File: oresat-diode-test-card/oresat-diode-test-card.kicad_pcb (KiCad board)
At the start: 4 copper layers, 99.8 x 94.6 mm, 140 parts, among them J6 J-SAMTEC-TFM-120-X1-XXX-D-RA, J7 ORESAT-DEBUG-CONNECTOR-ALL, Q1 DMP2240UDM, Q2 DMP3050LVT-7, Q4 DMP3050LVT-7, Q5 PMV45EN, Q7 MOSFET-PCH-SOT23-6, Q8 PMV45EN, Q9 PMV45EN, U1 TCAN330, U10 TPS62111RSA, U11 MIC842LYC5, U12 MIC842LYC5, U13 TLV6001DCK, U2 MAX7310, U3 TS5A21366DCUR, U4 TLV6001DCK, U6 MAX4211, U7 STM32F091C, U8 NX3L4051-Q100, U9 TLV6001DCK, X2 CRYSTAL-WITH-GND

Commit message: another layout rev
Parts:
- moved C6 14.5 mm to (135.3, 106.3), turned to 90 degrees
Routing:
- net Net-(D1-A): track 0.00 -> 78.3 mm, vias 0 -> 3
- net 3.3V: track 10.2 -> 73.0 mm, vias 13 -> 19
- net Net-(U5-1460nm): track 0.00 -> 39.2 mm, vias 0 -> 2
- net Net-(U5-1550nm): track 0.00 -> 38.6 mm, vias 0 -> 3
- net Net-(U5-1300nm): track 0.00 -> 31.8 mm
- net Net-(U5-1200nm): track 0.00 -> 30.5 mm, vias 0 -> 2
- net Net-(U5-1040nm): track 0.00 -> 28.9 mm, vias 0 -> 2
- net Net-(D2-K): track 9.52 -> 31.3 mm
- net Net-(D4-K): track 11.2 -> 26.5 mm
- net LED_CURRENT: track 61.8 -> 76.6 mm, vias 2 -> 3
- net Net-(U5-PD_Cathode): track 0.00 -> 9.51 mm
- net Net-(D1-K): track 12.2 -> 19.4 mm
- net SWIR_PD_CURRENT: track 68.9 -> 75.2 mm
- net ~{LED_MUX_ENABLE}: track 93.4 -> 90.4 mm
- net Net-(D8-K): track 2.63 -> 5.00 mm
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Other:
- board text added: "*:.｡.o(≧▽≦)o.｡.:*"
- board text added: "HAVE FUN! <3"
- board text added: "k"
- board text added: "m"
- board text added: "ori"
- board text added: "s"

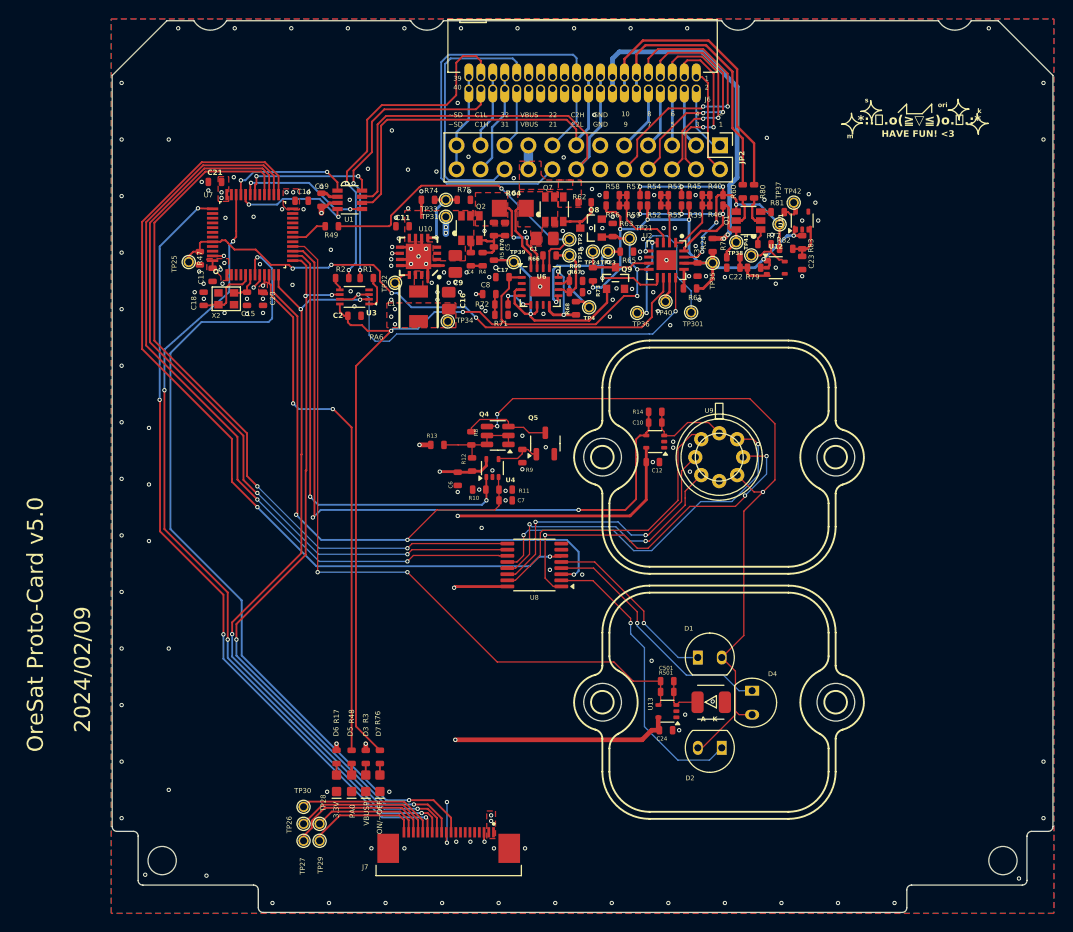
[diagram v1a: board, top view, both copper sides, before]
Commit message: Fix DRCs, clean up some routing, fix footprint movement on OPD.
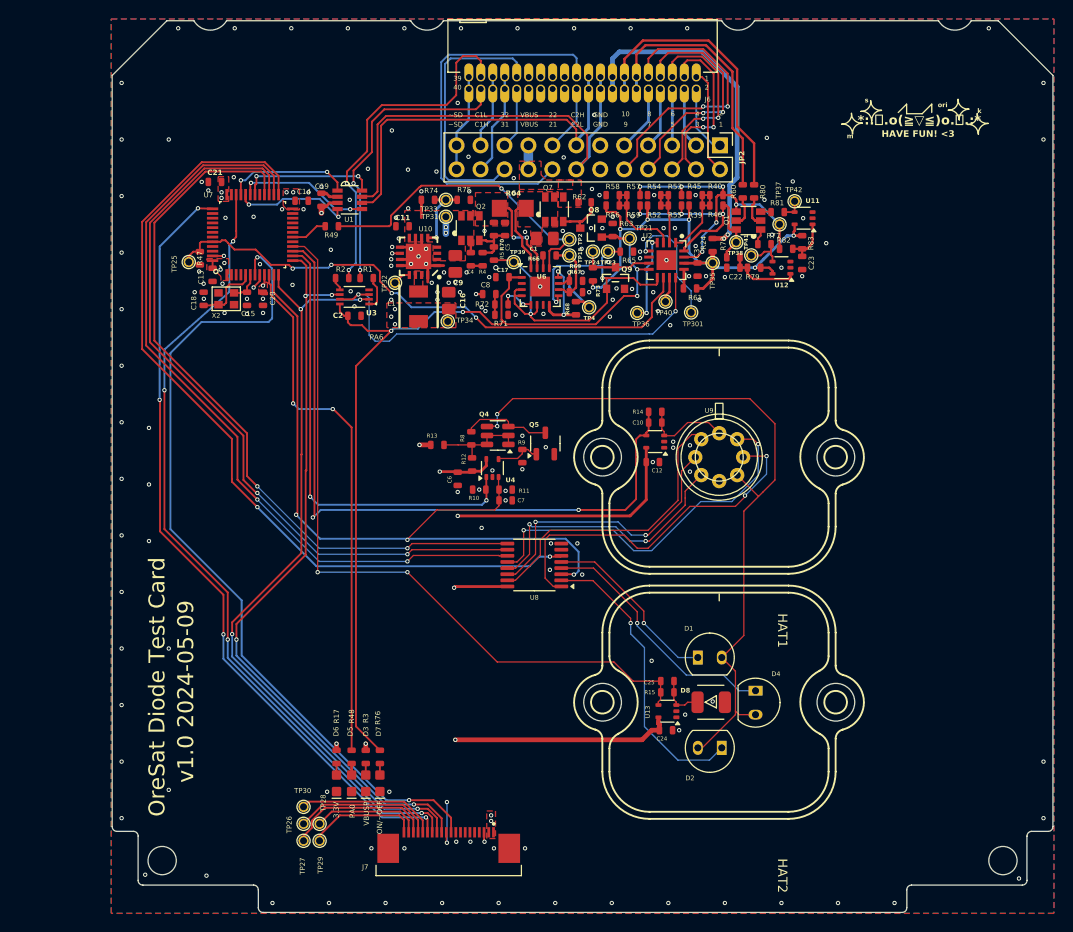
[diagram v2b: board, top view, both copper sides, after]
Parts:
- removed C501: 100n, oresat-passives:0603-C-NOSILK
- removed R501: 10K, oresat-passives:0603-C-NOSILK
- added C25: 100n, oresat-passives:0603-C-NOSILK, F.Cu at (157.5, 128.9)
- added R15: 10K, oresat-passives:0603-C-NOSILK, F.Cu at (157.5, 127.8)
- moved U12 0.60 mm to (169.6, 83.9), turned to 180 degrees
- moved D4 0.36 mm to (166.8, 128.8)
- moved U11 0.29 mm to (171.9, 78.7), turned to 180 degrees
- moved TP42 0.18 mm to (171.0, 76.8)
- renumbered REF** to HAT1, REF** to HAT2
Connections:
- Q9 pad 1: /Power/CB_CTRL -> /Power/CB-RESET
- R5 pad 1: /Power/CB_CTRL -> /Power/CB-RESET
- TP39 pad 1: /Power/CB_CTRL -> /Power/CB-RESET
- U6 pad 3: /Power/CB_CTRL -> /Power/CB-RESET
- U6 pad 4: /Power/CB_CTRL -> /Power/CB-RESET
- U6 pad 6: /Power/CB_CTRL -> /Power/CB-RESET
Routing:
- net /Power/CB-RESET: track 20.8 -> 48.1 mm, vias 2 -> 3
- net /Power/CB_CTRL: track 26.1 -> 0.00 mm, vias 1 -> 0
- net Net-(U12-INP): track 4.95 -> 7.73 mm
- net Net-(U5-1550nm): track 38.6 -> 38.4 mm, vias 3 -> 2
- net Net-(D1-A): track 78.3 -> 78.4 mm, vias 3 -> 2
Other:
- board text added: "${REVISION} ${ISSUE_DATE}"
- board text added: "OreSat Diode Test Card"
- board text removed: "2024/02/09"
- board text removed: "A K"
- board text removed: "OreSat Proto-Card v5.0"

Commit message: added test points and trace width edits
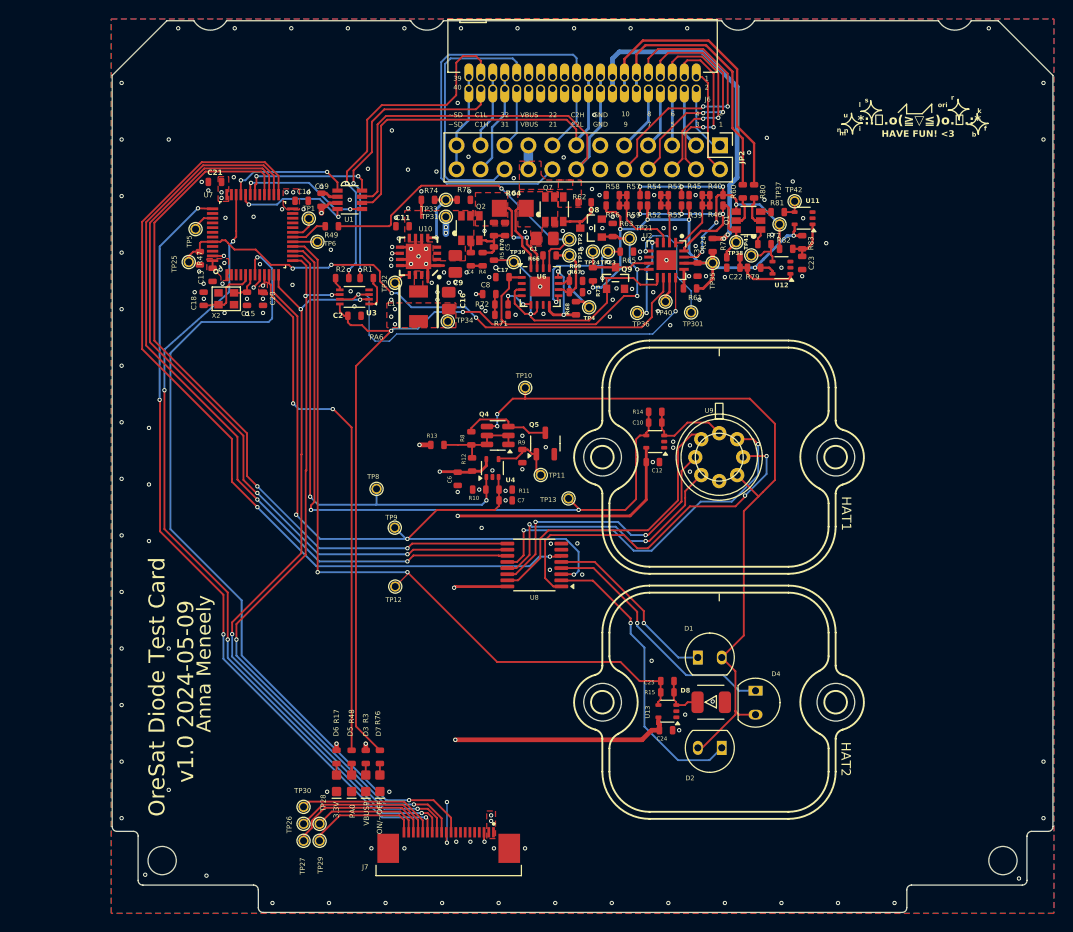
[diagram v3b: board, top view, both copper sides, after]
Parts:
- added TP1: TEST-POINT-LARGE-SQUARE, oresat-proto-card:1X01, F.Cu at (119.5, 78.7)
- added TP10: TEST-POINT-LARGE-SQUARE, oresat-proto-card:1X01, F.Cu at (142.4, 96.6)
- added TP11: TEST-POINT-LARGE-SQUARE, oresat-proto-card:1X01, F.Cu at (144.1, 105.9)
- added TP12: TEST-POINT-LARGE-SQUARE, oresat-proto-card:1X01, F.Cu at (128.6, 117.7)
- added TP13: TEST-POINT-LARGE-SQUARE, oresat-proto-card:1X01, F.Cu at (147.0, 108.4)
- added TP5: TEST-POINT-LARGE-SQUARE, oresat-proto-card:1X01, F.Cu at (107.4, 79.8)
- added TP6: TEST-POINT-LARGE-SQUARE, oresat-proto-card:1X01, F.Cu at (120.4, 81.2)
- added TP8: TEST-POINT-LARGE-SQUARE, oresat-proto-card:1X01, F.Cu at (126.6, 107.4)
- added TP9: TEST-POINT-LARGE-SQUARE, oresat-proto-card:1X01, F.Cu at (128.6, 111.5)
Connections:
- U7 pad 17: unconnected-(U7-PA7-Pad17) -> Net-(U7-PA7)
- U7 pad 19: unconnected-(U7-PB1-Pad19) -> Net-(U7-PB1)
- U7 pad 39: unconnected-(U7-PB3-Pad39) -> Net-(U7-PB3)
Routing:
- net Net-(U7-PB1): track 0.00 -> 2.80 mm
- net Net-(U7-PA7): track 0.00 -> 2.62 mm
- net Net-(U7-PB3): track 0.00 -> 2.45 mm
- net Net-(Q5-G): track 4.90 -> 7.23 mm
- net UV_PD_CURRENT: track 80.2 -> 82.2 mm
- net LED_CURRENT: track 76.6 -> 78.4 mm
- net DAC_OUT: track 48.7 -> 50.4 mm
- net Net-(D1-A): track 78.4 -> 79.5 mm
- net SWIR_PD_CURRENT: track 75.2 -> 76.0 mm
- net GND: vias 188 -> 189
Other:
- board text added: "Anna Meneely"
- board text added: "b"
- board text added: "f"
- board text added: "i"
- board text added: "l"
- board text added: "n"
- board text added: "r"
- board text added: "u"

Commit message: Fix OPD weirdness, lots of little polishing including power plane movement and thicker traces.
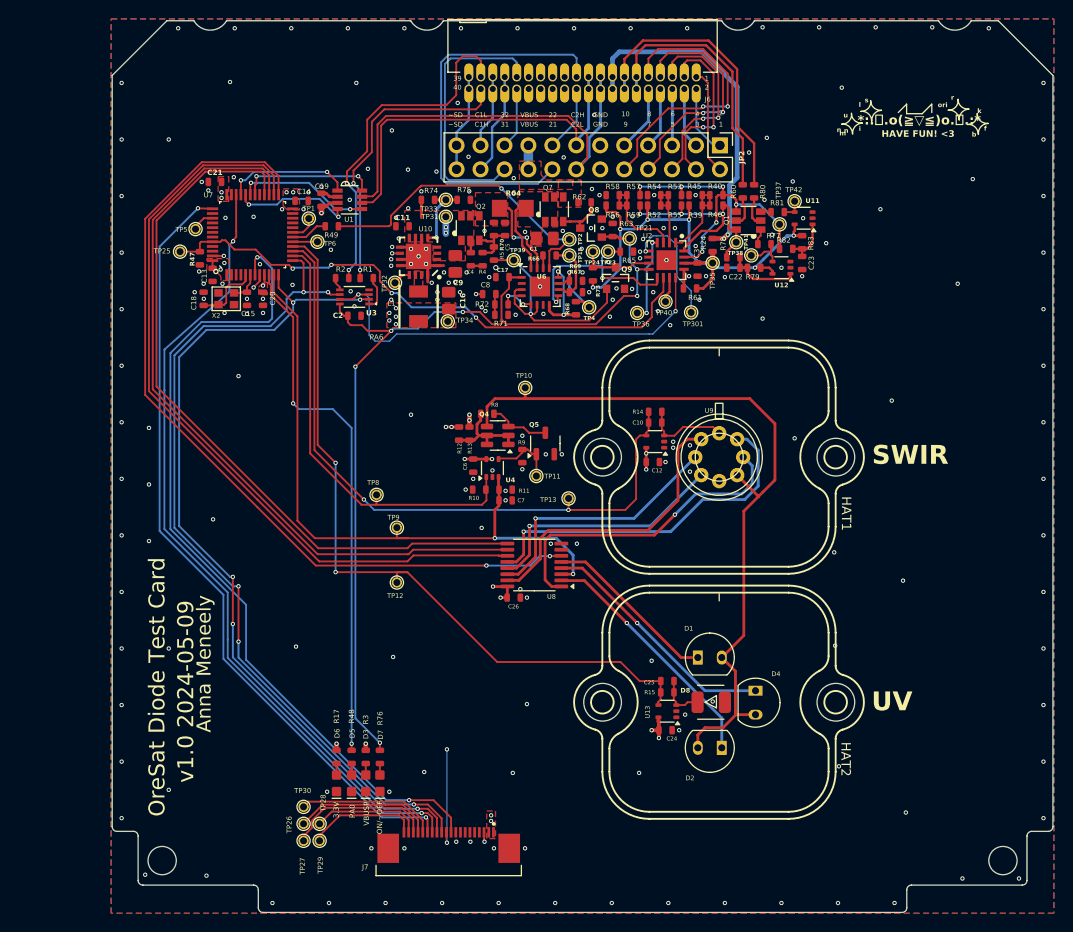
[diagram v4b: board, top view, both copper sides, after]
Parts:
- added C26: 100n, oresat-passives:0603-C-NOSILK, F.Cu at (141.2, 118.9)
- moved R13 3.61 mm to (136.5, 101.5), turned to 90 degrees
- moved R12 3.55 mm to (135.4, 101.5), turned to 90 degrees
- moved R8 3.11 mm to (138.4, 99.4), turned to 180 degrees
- moved C6 2.16 mm to (136.9, 104.9)
- moved TP25 1.43 mm to (105.8, 82.2)
- moved TP8 0.63 mm to (126.6, 108.0)
- moved TP11 0.48 mm to (143.6, 106.0)
- moved TP12 0.46 mm to (128.8, 117.3)
- moved TP9 0.23 mm to (128.8, 111.5)
- moved TP39 0.20 mm to (141.2, 83.1)
- moved C24 0.05 mm to (157.3, 133.0)
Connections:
- Q9 pad 1: /Power/CB-RESET -> /Power/CB_CTRL
- R5 pad 1: /Power/CB-RESET -> /Power/CB_CTRL
- TP39 pad 1: /Power/CB-RESET -> /Power/CB_CTRL
- U6 pad 3: /Power/CB-RESET -> /Power/CB_CTRL
- U6 pad 4: /Power/CB-RESET -> /Power/CB_CTRL
- U6 pad 6: /Power/CB-RESET -> /Power/CB_CTRL
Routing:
- net 3.3V: track 73.0 -> 30.4 mm, vias 19 -> 27
- net /Power/CB-RESET: track 48.1 -> 20.8 mm, vias 3 -> 2
- net /Power/CB_CTRL: track 0.00 -> 26.1 mm, vias 0 -> 1
- net PA3/USART2_RX: track 80.3 -> 90.8 mm, vias 4 -> 5
- net PA2/USART2_TX: track 82.6 -> 91.4 mm, vias 4 -> 5
- net LED_CURRENT: track 78.4 -> 70.3 mm, vias 3 -> 2
- net Net-(D2-K): track 31.3 -> 26.2 mm
- net SWIR_PD_CURRENT: track 76.0 -> 71.4 mm
- net Net-(U5-1550nm): track 38.3 -> 33.9 mm, vias 2 -> 1
- net VBUSP: track 26.7 -> 22.5 mm, vias 7 -> 8
- net DAC_OUT: track 50.4 -> 47.1 mm, vias 2 -> 0
- net Net-(Q4-G): track 9.51 -> 6.58 mm
- net Net-(U5-1200nm): track 30.2 -> 27.5 mm, vias 2 -> 1
- net Net-(U5-1040nm): track 28.9 -> 26.5 mm, vias 2 -> 1
- net Net-(U5-1460nm): track 39.5 -> 37.9 mm, vias 2 -> 1
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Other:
- board text added: "SWIR"
- board text added: "UV"

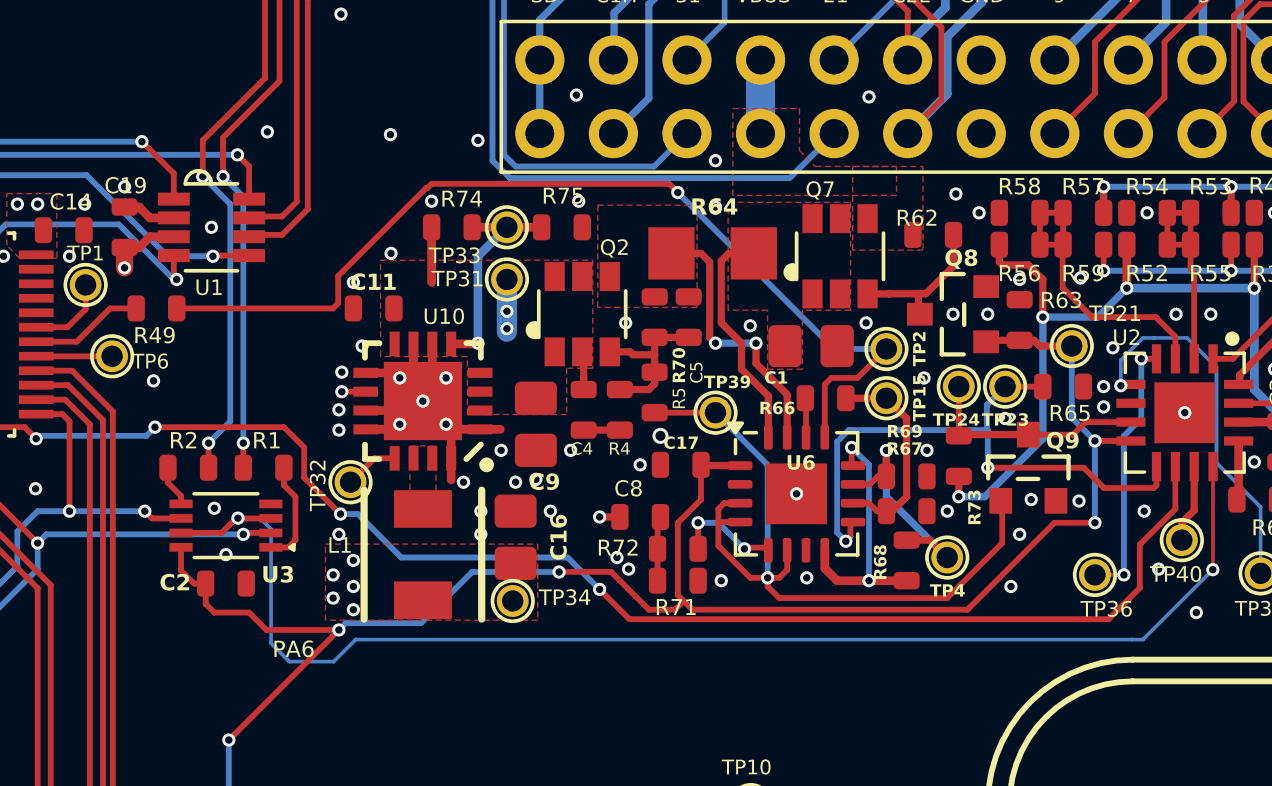
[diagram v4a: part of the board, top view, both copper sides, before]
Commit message: BOM changes! Now up to date.
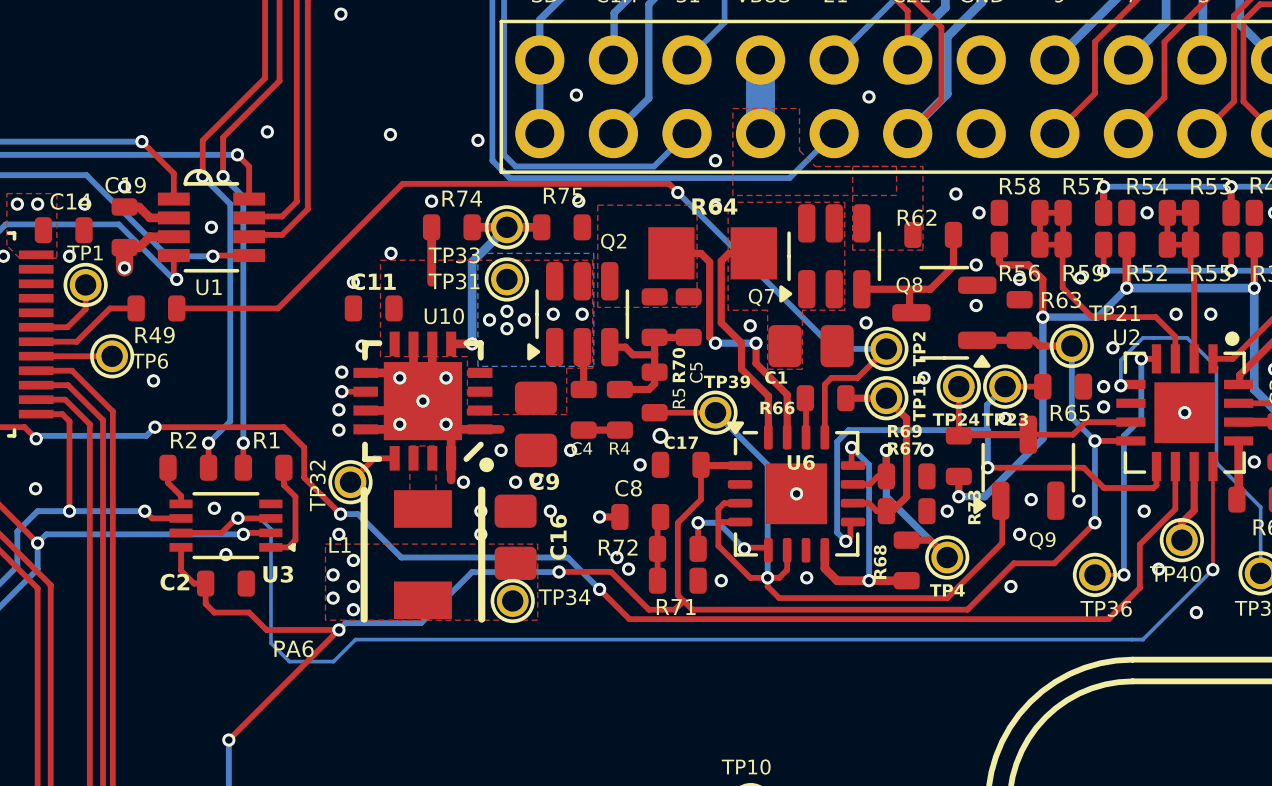
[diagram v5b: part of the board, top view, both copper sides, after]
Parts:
- C2: value CL10B104KB8NNNL -> 100n
- D1: value LED -> 378 nm UV - MY5375-UV
- D2: value LED -> 300 nm UV - MT0380-UV-A
- D4: value LED -> UV LED - TBD!
- D8: value D_Photo -> GVBL-S12SD
- JP2: value PINHD-2X5 -> PINHD-2X12
- Q2: footprint oresat-proto-card:SOT23-6 -> Package_TO_SOT_SMD:SOT-23-6
- Q7: value MOSFET-PCH-SOT23-6 -> DMP3050LVT-7; footprint oresat-proto-card:SOT23-6 -> Package_TO_SOT_SMD:SOT-23-6
- Q8, Q9: footprint oresat-proto-card:SOT23 -> Package_TO_SOT_SMD:SOT-23-3
- R10, R14, R15, R72, R8, R9: value 10K -> 10k
- R4, R5: value RC0603FR-0710KL -> 10k
- U5: value ~ -> MTMD142345PDT38
- moved Q8 0.30 mm to (149.1, 79.7), turned to 180 degrees
- moved Q7 0.20 mm to (145.3, 77.7), turned to 90 degrees
- turned Q2 to 90 degrees
- turned Q9 to 90 degrees
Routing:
- net VBUSP: track 22.5 -> 20.7 mm, vias 8 -> 12
- net POUT: track 33.7 -> 33.2 mm
- net GND: vias 228 -> 227
- added copper zone on B.Cu, net VBUSP
